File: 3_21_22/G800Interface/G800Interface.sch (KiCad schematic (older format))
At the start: 27 parts

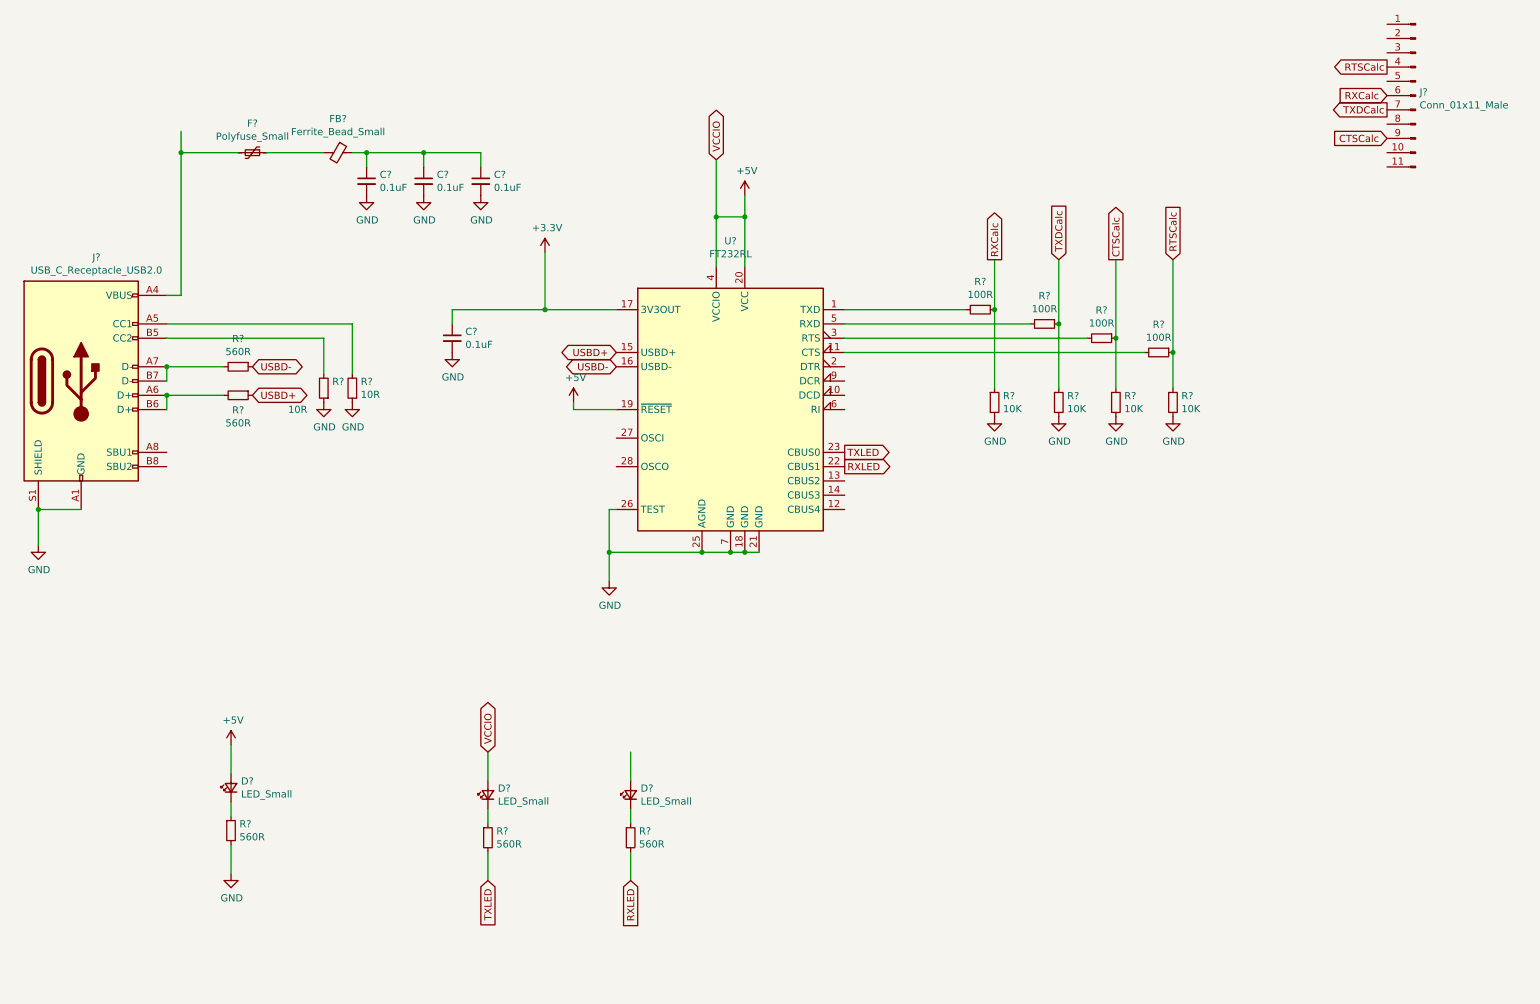
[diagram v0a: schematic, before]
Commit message: Routing G800 Interface
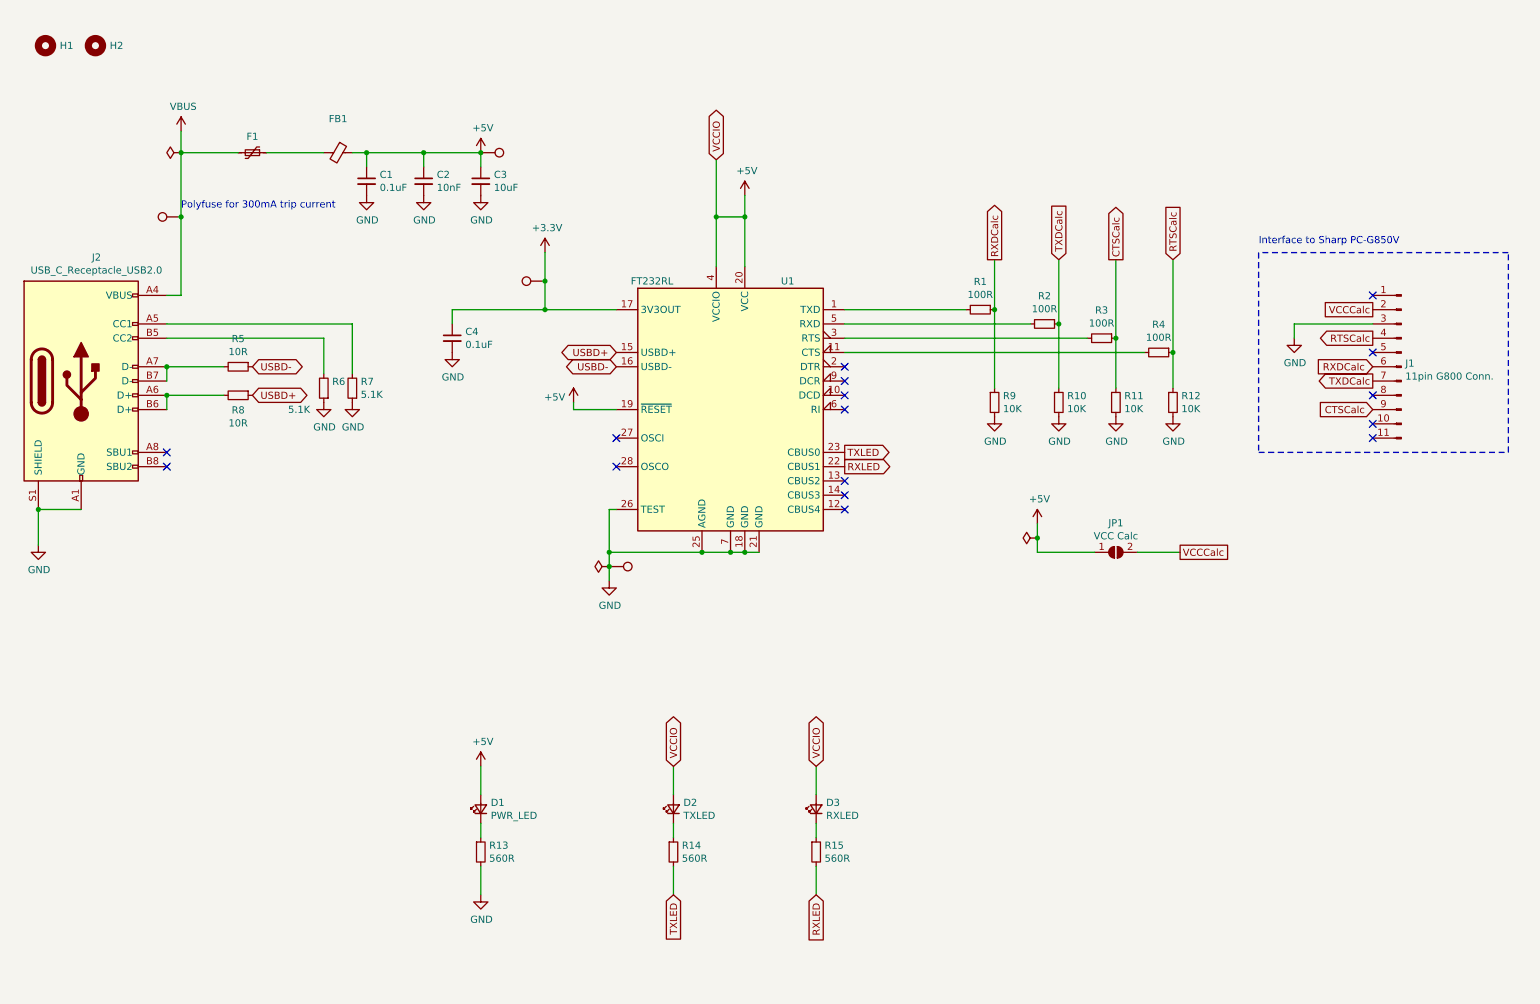
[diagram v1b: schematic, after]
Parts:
- added H1, H2: MountingHole, MountingHole:MountingHole_3mm, symbol Mechanical:MountingHole
- added JP1: VCC Calc, Jumper:SolderJumper-2_P1.3mm_Open_RoundedPad1.0x1.5mm, symbol Jumper:SolderJumper_2_Open
- added TP1: tp5V, TestPoint:TestPoint_Pad_D2.0mm, symbol Connector:TestPoint
- added TP2: tpVBUS, TestPoint:TestPoint_Pad_D2.0mm, symbol Connector:TestPoint
- added TP3: tp3V3, TestPoint:TestPoint_Pad_D2.0mm, symbol Connector:TestPoint
- added TP4: tpGND, TestPoint:TestPoint_Pad_D2.0mm, symbol Connector:TestPoint
- C1, C4: renamed from C?; footprint (none) -> Capacitor_SMD:C_0805_2012Metric
- C2: renamed from C?; value 0.1uF -> 10nF; footprint (none) -> Capacitor_SMD:C_0805_2012Metric
- C3: renamed from C?; value 0.1uF -> 10uF; footprint (none) -> Capacitor_SMD:C_0805_2012Metric
- D1: renamed from D?; value LED_Small -> PWR_LED; footprint (none) -> LED_SMD:LED_0805_2012Metric
- D2: renamed from D?; value LED_Small -> TXLED; footprint (none) -> LED_SMD:LED_0805_2012Metric
- D3: renamed from D?; value LED_Small -> RXLED; footprint (none) -> LED_SMD:LED_0805_2012Metric
- F1: renamed from F?; footprint (none) -> Fuse:Fuse_1812_4532Metric
- FB1: renamed from FB?; footprint (none) -> Inductor_SMD:L_0805_2012Metric
- J1: renamed from J?; value Conn_01x11_Male -> 11pin G800 Conn.; footprint (none) -> Connector_PinHeader_2.54mm:PinHeader_1x11_P2.54mm_Horizontal
- J2: renamed from J?; footprint (none) -> Connector_USB:USB_C_Receptacle_HRO_TYPE-C-31-M-12
- R1, R10, R11, R12, R13, R14, R15, R2, R3, R4, R9: renamed from R?; footprint (none) -> Resistor_SMD:R_0805_2012Metric
- R5, R8: renamed from R?; value 560R -> 10R; footprint (none) -> Resistor_SMD:R_0805_2012Metric
- R6, R7: renamed from R?; value 10R -> 5.1K; footprint (none) -> Resistor_SMD:R_0805_2012Metric
- gave numbers to parts that had none: 1
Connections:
- net labels added: RXDCalc, VBUS, VCCCalc
- net labels removed: RXCalc
- wire segments 60 -> 69
- no-connect marks 0 -> 16
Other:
- note added: "Interface to Sharp PC-G850V"
- note added: "Polyfuse for 300mA trip current"
- moved on the sheet: D1, D2, D3, J1, R13, R14, R15

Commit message: diff pair + decoupling C
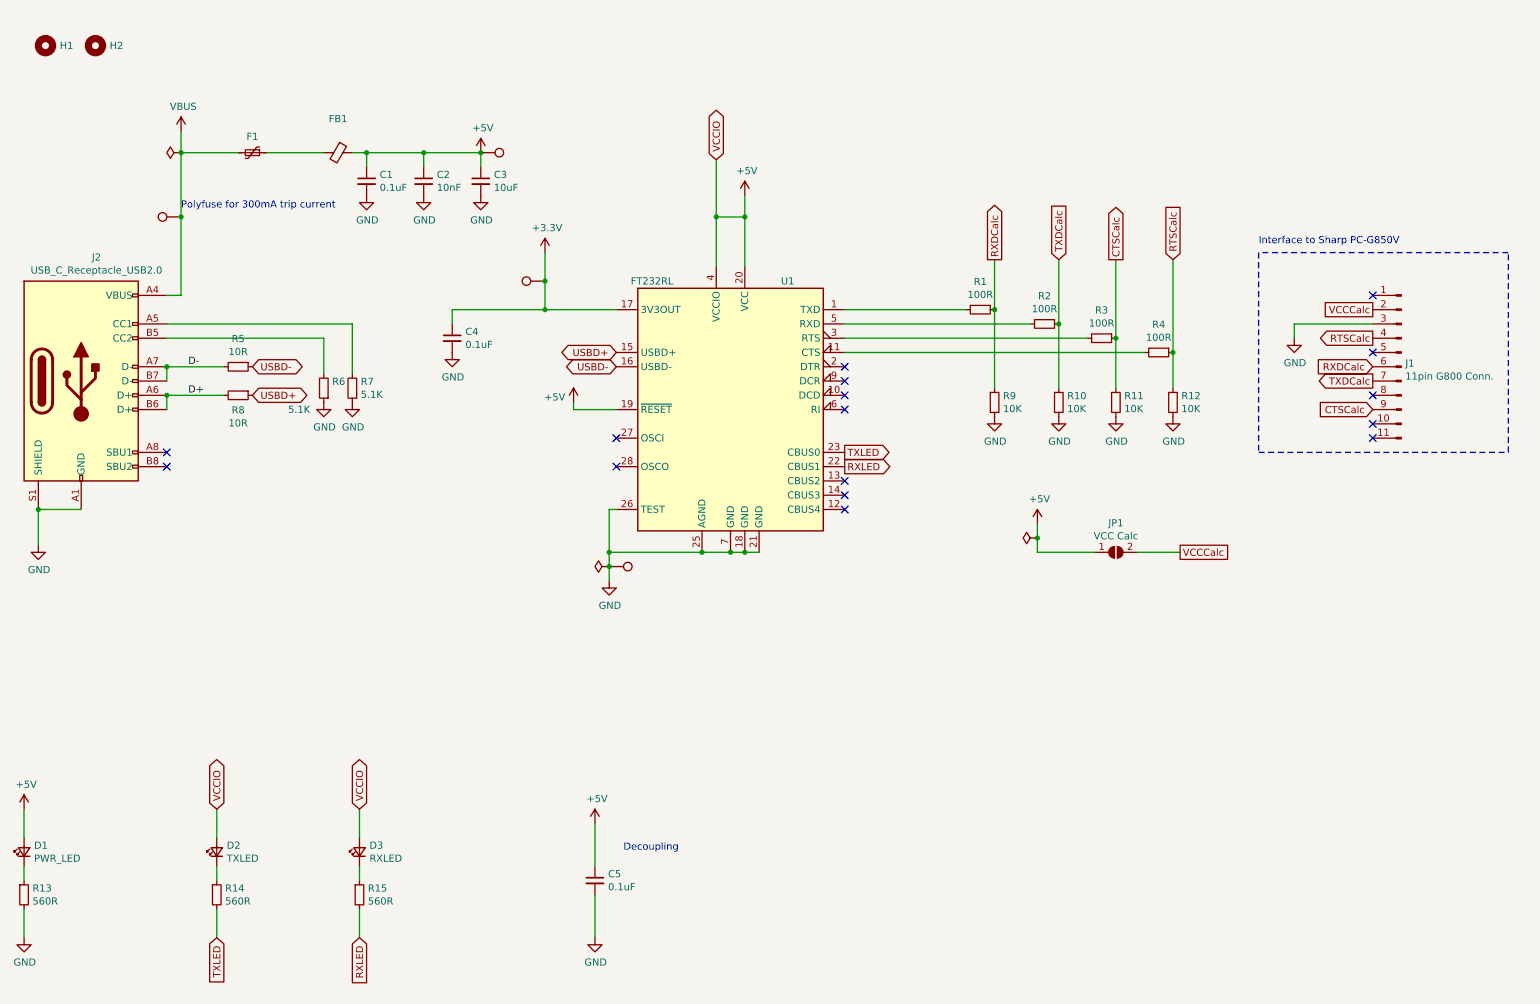
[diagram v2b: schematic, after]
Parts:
- added C5: 0.1uF, Capacitor_SMD:C_0805_2012Metric, symbol Device:C_Small
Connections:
- net +5V: now also C5.1
- net GND: now also C5.2
- net D+: now reaches J2.A6 (D+), J2.B6 (D+), R8.2
- net D-: now reaches J2.A7 (D-), J2.B7 (D-), R5.2
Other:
- note added: "Decoupling"
- moved on the sheet: D1, D2, D3, R13, R14, R15
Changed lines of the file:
@@
 	1    0    0    -1
 $EndComp
-$Comp
-L Device:LED_Small D1
-U 1 1 613AA9EB
-P 3950 6550
-F 0 "D1" V 3996 6480 50  0000 R CNN
-F 1 "PWR_LED" V 3905 6480 50  0000 R CNN
-F 2 "LED_SMD:LED_0805_2012Metric" V 3950 6550 50  0001 C CNN
-F 3 "~" V 3950 6550 50  0001 C CNN
-	1    3950 6550
-	0    -1   -1   0
-$EndComp
-$Comp
-L Device:R_Small R13
-U 1 1 613AB406
-P 3950 6850
-F 0 "R13" H 4009 6896 50  0000 L CNN
-F 1 "560R" H 4009 6805 50  0000 L CNN
-F 2 "Resistor_SMD:R_0805_2012Metric" H 3950 6850 50  0001 C CNN
-F 3 "~" H 3950 6850 50  0001 C CNN
-	1    3950 6850
-	1    0    0    -1
-$EndComp
-Wire Wire Line
-	3950 6750 3950 6650
-Wire Wire Line
-	3950 6450 3950 6250
-Wire Wire Line
-	3950 6950 3950 7150
-$Comp
-L power:+5V #PWR020
-U 1 1 613ABA73
-P 3950 6250
-F 0 "#PWR020" H 3950 6100 50  0001 C CNN
-F 1 "+5V" H 3965 6423 50  0000 C CNN
-F 2 "" H 3950 6250 50  0001 C CNN
-F 3 "" H 3950 6250 50  0001 C CNN
-	1    3950 6250
-	1    0    0    -1
-$EndComp
-$Comp
-L power:GND #PWR021
-U 1 1 613AC2C1
-P 3950 7150
-F 0 "#PWR021" H 3950 6900 50  0001 C CNN
-F 1 "GND" H 3955 6977 50  0000 C CNN
-F 2 "" H 3950 7150 50  0001 C CNN
-F 3 "" H 3950 7150 50  0001 C CNN
-	1    3950 7150
-	1    0    0    -1
-$EndComp
-$Comp
-L Device:LED_Small D2
-U 1 1 613AC956
-P 5300 6550
-F 0 "D2" V 5346 6480 50  0000 R CNN
-F 1 "TXLED" V 5255 6480 50  0000 R CNN
-F 2 "LED_SMD:LED_0805_2012Metric" V 5300 6550 50  0001 C CNN
-F 3 "~" V 5300 6550 50  0001 C CNN
-	1    5300 6550
-	0    -1   -1   0
-$EndComp
-$Comp
-L Device:LED_Small D3
-U 1 1 613AD086
-P 6300 6550
-F 0 "D3" V 6346 6480 50  0000 R CNN
-F 1 "RXLED" V 6255 6480 50  0000 R CNN
-F 2 "LED_SMD:LED_0805_2012Metric" V 6300 6550 50  0001 C CNN
-F 3 "~" V 6300 6550 50  0001 C CNN
-	1    6300 6550
-	0    -1   -1   0
-$EndComp
-$Comp
-L Device:R_Small R14
-U 1 1 613AD46C
-P 5300 6850
-F 0 "R14" H 5359 6896 50  0000 L CNN
-F 1 "560R" H 5359 6805 50  0000 L CNN
-F 2 "Resistor_SMD:R_0805_2012Metric" H 5300 6850 50  0001 C CNN
-F 3 "~" H 5300 6850 50  0001 C CNN
-	1    5300 6850
-	1    0    0    -1
-$EndComp
-$Comp
-L Device:R_Small R15
-U 1 1 613AD90A
-P 6300 6850
-F 0 "R15" H 6359 6896 50  0000 L CNN
-F 1 "560R" H 6359 6805 50  0000 L CNN
-F 2 "Resistor_SMD:R_0805_2012Metric" H 6300 6850 50  0001 C CNN
-F 3 "~" H 6300 6850 50  0001 C CNN
-	1    6300 6850
-	1    0    0    -1
-$EndComp
-Wire Wire Line
-	5300 6750 5300 6650
-Wire Wire Line
-	6300 6750 6300 6650
-Wire Wire Line
-	5300 6450 5300 6250
-Wire Wire Line
-	6300 6450 6300 6250
-Wire Wire Line
-	5300 6950 5300 7150
 Text GLabel 6500 4050 2    50   Output ~ 0
-TXLED
-Text GLabel 5300 7150 3    50   Input ~ 0
 TXLED
 Text GLabel 6500 4150 2    50   Output ~ 0
 RXLED
-Text GLabel 6300 7150 3    50   Input ~ 0
-RXLED
-Wire Wire Line
-	6300 6950 6300 7150
 Wire Wire Line
 	6500 3050 7350 3050
@@
 Wire Wire Line
 	5600 2750 5600 2400
-Text GLabel 5300 6250 1    50   BiDi ~ 0
-VCCIO
 Text GLabel 5600 2000 1    50   BiDi ~ 0
 VCCIO
@@
 	1    0    0    -1
 $EndComp
-Text GLabel 6300 6250 1    50   BiDi ~ 0
-VCCIO
 NoConn ~ 10200 2950
 NoConn ~ 10200 3350
@@
 Text Notes 9400 2600 0    50   ~ 0
 Interface to Sharp PC-G850V
+Text GLabel 3100 6550 1    50   BiDi ~ 0
+VCCIO
+Text GLabel 2100 6550 1    50   BiDi ~ 0
+VCCIO
+Wire Wire Line
+	3100 7250 3100 7450
+Text GLabel 3100 7450 3    50   Input ~ 0
+RXLED
+Text GLabel 2100 7450 3    50   Input ~ 0
+TXLED
+Wire Wire Line
+	2100 7250 2100 7450
+Wire Wire Line
+	3100 6750 3100 6550
+Wire Wire Line
+	2100 6750 2100 6550
+Wire Wire Line
+	3100 7050 3100 6950
+Wire Wire Line
+	2100 7050 2100 6950
+$Comp
+L Device:R_Small R15
+U 1 1 613AD90A
+P 3100 7150
+F 0 "R15" H 3159 7196 50  0000 L CNN
+F 1 "560R" H 3159 7105 50  0000 L CNN
+F 2 "Resistor_SMD:R_0805_2012Metric" H 3100 7150 50  0001 C CNN
+F 3 "~" H 3100 7150 50  0001 C CNN
+	1    3100 7150
+	1    0    0    -1
+$EndComp
+$Comp
+L Device:R_Small R14
+U 1 1 613AD46C
+P 2100 7150
+F 0 "R14" H 2159 7196 50  0000 L CNN
+F 1 "560R" H 2159 7105 50  0000 L CNN
+F 2 "Resistor_SMD:R_0805_2012Metric" H 2100 7150 50  0001 C CNN
+F 3 "~" H 2100 7150 50  0001 C CNN
+	1    2100 7150
+	1    0    0    -1
+$EndComp
+$Comp
+L Device:LED_Small D3
+U 1 1 613AD086
+P 3100 6850
+F 0 "D3" V 3146 6780 50  0000 R CNN
+F 1 "RXLED" V 3055 6780 50  0000 R CNN
+F 2 "LED_SMD:LED_0805_2012Metric" V 3100 6850 50  0001 C CNN
+F 3 "~" V 3100 6850 50  0001 C CNN
+	1    3100 6850
+	0    -1   -1   0
+$EndComp
+$Comp
+L Device:LED_Small D2
+U 1 1 613AC956
+P 2100 6850
+F 0 "D2" V 2146 6780 50  0000 R CNN
+F 1 "TXLED" V 2055 6780 50  0000 R CNN
+F 2 "LED_SMD:LED_0805_2012Metric" V 2100 6850 50  0001 C CNN
+F 3 "~" V 2100 6850 50  0001 C CNN
+	1    2100 6850
+	0    -1   -1   0
+$EndComp
+$Comp
+L power:GND #PWR021
+U 1 1 613AC2C1
+P 750 7450
+F 0 "#PWR021" H 750 7200 50  0001 C CNN
+F 1 "GND" H 755 7277 50  0000 C CNN
+F 2 "" H 750 7450 50  0001 C CNN
+F 3 "" H 750 7450 50  0001 C CNN
+	1    750  7450
+	1    0    0    -1
+$EndComp
+$Comp
+L power:+5V #PWR020
+U 1 1 613ABA73
+P 750 6550
+F 0 "#PWR020" H 750 6400 50  0001 C CNN
+F 1 "+5V" H 765 6723 50  0000 C CNN
+F 2 "" H 750 6550 50  0001 C CNN
+F 3 "" H 750 6550 50  0001 C CNN
+	1    750  6550
+	1    0    0    -1
+$EndComp
+Wire Wire Line
+	750  7250 750  7450
+Wire Wire Line
+	750  6750 750  6550
+Wire Wire Line
+	750  7050 750  6950
+$Comp
+L Device:R_Small R13
+U 1 1 613AB406
+P 750 7150
+F 0 "R13" H 809 7196 50  0000 L CNN
+F 1 "560R" H 809 7105 50  0000 L CNN
+F 2 "Resistor_SMD:R_0805_2012Metric" H 750 7150 50  0001 C CNN
+F 3 "~" H 750 7150 50  0001 C CNN
+	1    750  7150
+	1    0    0    -1
+$EndComp
+$Comp
+L Device:LED_Small D1
+U 1 1 613AA9EB
+P 750 6850
+F 0 "D1" V 796 6780 50  0000 R CNN
+F 1 "PWR_LED" V 705 6780 50  0000 R CNN
+F 2 "LED_SMD:LED_0805_2012Metric" V 750 6850 50  0001 C CNN
+F 3 "~" V 750 6850 50  0001 C CNN
+	1    750  6850
+	0    -1   -1   0
+$EndComp
+$Comp
+L Device:C_Small C5
+U 1 1 61449614
+P 4750 7050
+F 0 "C5" H 4842 7096 50  0000 L CNN
+F 1 "0.1uF" H 4842 7005 50  0000 L CNN
+F 2 "Capacitor_SMD:C_0805_2012Metric" H 4750 7050 50  0001 C CNN
+F 3 "~" H 4750 7050 50  0001 C CNN
+	1    4750 7050
+	1    0    0    -1
+$EndComp
+Wire Wire Line
+	4750 6950 4750 6650
+Wire Wire Line
+	4750 7150 4750 7450
+$Comp
+L power:GND #PWR023
+U 1 1 6144E1B6
+P 4750 7450
+F 0 "#PWR023" H 4750 7200 50  0001 C CNN
+F 1 "GND" H 4755 7277 50  0000 C CNN
+F 2 "" H 4750 7450 50  0001 C CNN
+F 3 "" H 4750 7450 50  0001 C CNN
+	1    4750 7450
+	1    0    0    -1
+$EndComp
+$Comp
+L power:+5V #PWR022
+U 1 1 6144E7D4
+P 4750 6650
+F 0 "#PWR022" H 4750 6500 50  0001 C CNN
+F 1 "+5V" H 4765 6823 50  0000 C CNN
+F 2 "" H 4750 6650 50  0001 C CNN
+F 3 "" H 4750 6650 50  0001 C CNN
+	1    4750 6650
+	1    0    0    -1
+$EndComp
+Text Notes 4950 6850 0    50   ~ 0
+Decoupling
+Text Label 1900 3450 0    50   ~ 0
+D-
+Text Label 1900 3650 0    50   ~ 0
+D+
 $EndSCHEMATC

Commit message: finished G800
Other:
- moved on the sheet: C5
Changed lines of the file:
@@
 L Device:C_Small C5
 U 1 1 61449614
-P 4750 7050
-F 0 "C5" H 4842 7096 50  0000 L CNN
-F 1 "0.1uF" H 4842 7005 50  0000 L CNN
-F 2 "Capacitor_SMD:C_0805_2012Metric" H 4750 7050 50  0001 C CNN
-F 3 "~" H 4750 7050 50  0001 C CNN
-	1    4750 7050
+P 6000 7100
+F 0 "C5" H 6092 7146 50  0000 L CNN
+F 1 "0.1uF" H 6092 7055 50  0000 L CNN
+F 2 "Capacitor_SMD:C_0805_2012Metric" H 6000 7100 50  0001 C CNN
+F 3 "~" H 6000 7100 50  0001 C CNN
+	1    6000 7100
 	1    0    0    -1
 $EndComp
 Wire Wire Line
-	4750 6950 4750 6650
+	6000 7000 6000 6700
 Wire Wire Line
-	4750 7150 4750 7450
+	6000 7200 6000 7500
 $Comp
 L power:GND #PWR023
 U 1 1 6144E1B6
-P 4750 7450
-F 0 "#PWR023" H 4750 7200 50  0001 C CNN
-F 1 "GND" H 4755 7277 50  0000 C CNN
-F 2 "" H 4750 7450 50  0001 C CNN
-F 3 "" H 4750 7450 50  0001 C CNN
-	1    4750 7450
+P 6000 7500
+F 0 "#PWR023" H 6000 7250 50  0001 C CNN
+F 1 "GND" H 6005 7327 50  0000 C CNN
+F 2 "" H 6000 7500 50  0001 C CNN
+F 3 "" H 6000 7500 50  0001 C CNN
+	1    6000 7500
 	1    0    0    -1
 $EndComp
@@
 L power:+5V #PWR022
 U 1 1 6144E7D4
-P 4750 6650
-F 0 "#PWR022" H 4750 6500 50  0001 C CNN
-F 1 "+5V" H 4765 6823 50  0000 C CNN
-F 2 "" H 4750 6650 50  0001 C CNN
-F 3 "" H 4750 6650 50  0001 C CNN
-	1    4750 6650
+P 6000 6700
+F 0 "#PWR022" H 6000 6550 50  0001 C CNN
+F 1 "+5V" H 6015 6873 50  0000 C CNN
+F 2 "" H 6000 6700 50  0001 C CNN
+F 3 "" H 6000 6700 50  0001 C CNN
+	1    6000 6700
 	1    0    0    -1
 $EndComp
-Text Notes 4950 6850 0    50   ~ 0
+Text Notes 6200 6900 0    50   ~ 0
 Decoupling
 Text Label 1900 3450 0    50   ~ 0
